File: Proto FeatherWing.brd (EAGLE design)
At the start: 50.8 x 22.9 mm, 3 parts

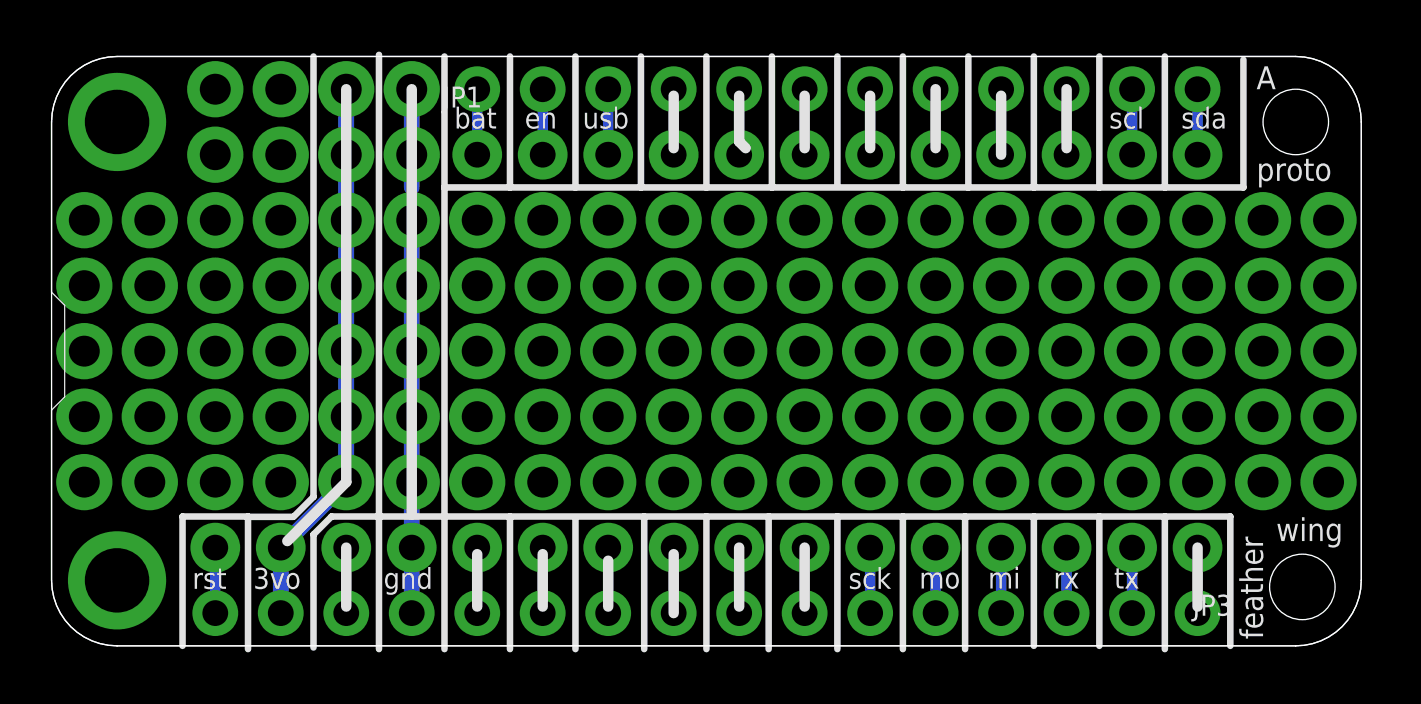
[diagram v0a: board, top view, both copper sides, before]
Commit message: fix minor hole location error - EN is now labeled EN
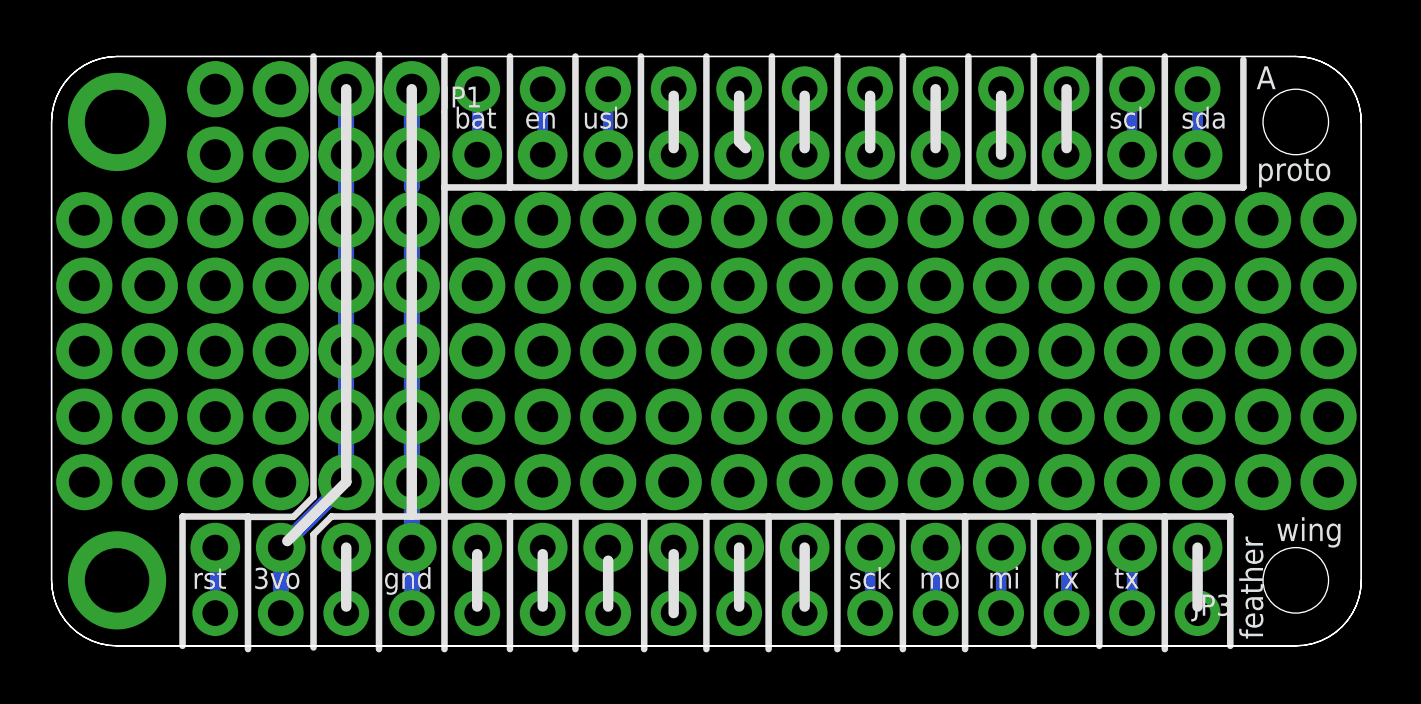
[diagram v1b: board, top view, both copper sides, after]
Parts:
- MS1: value MICROSHIELD_NODIM -> FEATHERWING; device microbuilder:MICROSHIELD_DIM -> microbuilder:FEATHERWING
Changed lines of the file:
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@@
 </autorouter>
 <elements>
-<element name="MS1" library="microbuilder" package="MICROSHIELD_DIM" value="MICROSHIELD_NODIM" x="0" y="0"/>
+<element name="MS1" library="microbuilder" package="FEATHERWING" value="FEATHERWING" x="0" y="0"/>
 <element name="JP3" library="microbuilder" package="1X16_ROUND_76MIL" value="" x="25.4" y="3.81" rot="R180"/>
 <element name="JP1" library="microbuilder" package="1X12_ROUND_76MIL" value="" x="30.48" y="19.05"/>
